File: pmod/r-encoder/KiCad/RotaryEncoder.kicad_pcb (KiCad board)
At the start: 2 copper layers, 39 x 39 mm, 15 parts, among them J1 Conn_01x06, U1 PEC11R-4325F-S0012

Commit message: fix: connectors
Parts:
- J1: footprint Connector_PinHeader_2.54mm:PinHeader_1x06_P2.54mm_Vertical -> Connector_PinHeader_2.54mm:PinHeader_1x06_P2.54mm_Horizontal
- moved J1 12.8 mm to (110.2, 80.1), turned to 180 degrees
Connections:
- J1 pad 1: A -> unconnected-(J1-Pin_1-Pad1)
- J1 pad 2: B -> BTN
- J1 pad 3: BTN -> B
- J1 pad 4: unconnected-(J1-Pin_4-Pad4) -> A
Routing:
- net GND: track 9.76 -> 0.00 mm, vias 17 -> 15
- net A: track 12.2 -> 17.3 mm
- net B: track 21.1 -> 17.7 mm
- net VCC: track 55.4 -> 54.8 mm
- net BTN: track 32.9 -> 33.2 mm, vias 0 -> 1

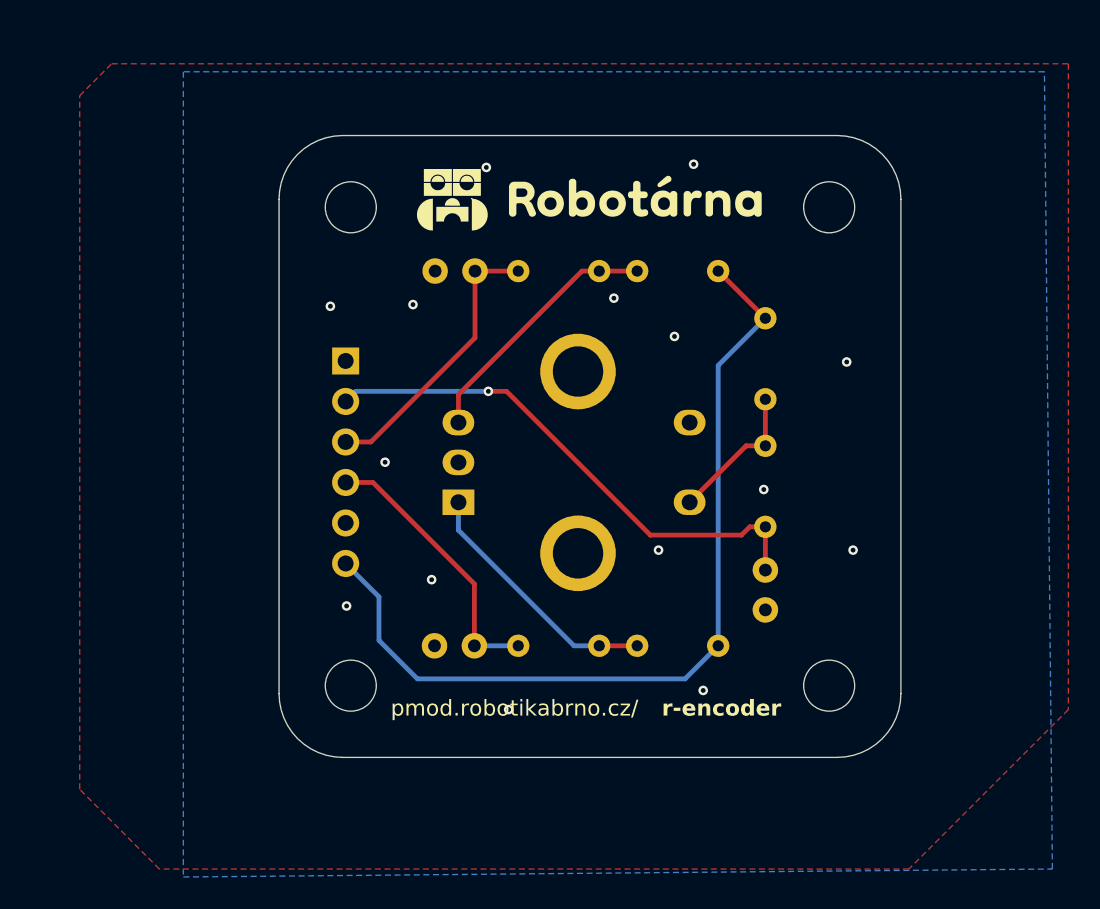
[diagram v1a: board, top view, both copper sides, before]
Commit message: fix: prepare all board for manufacturing
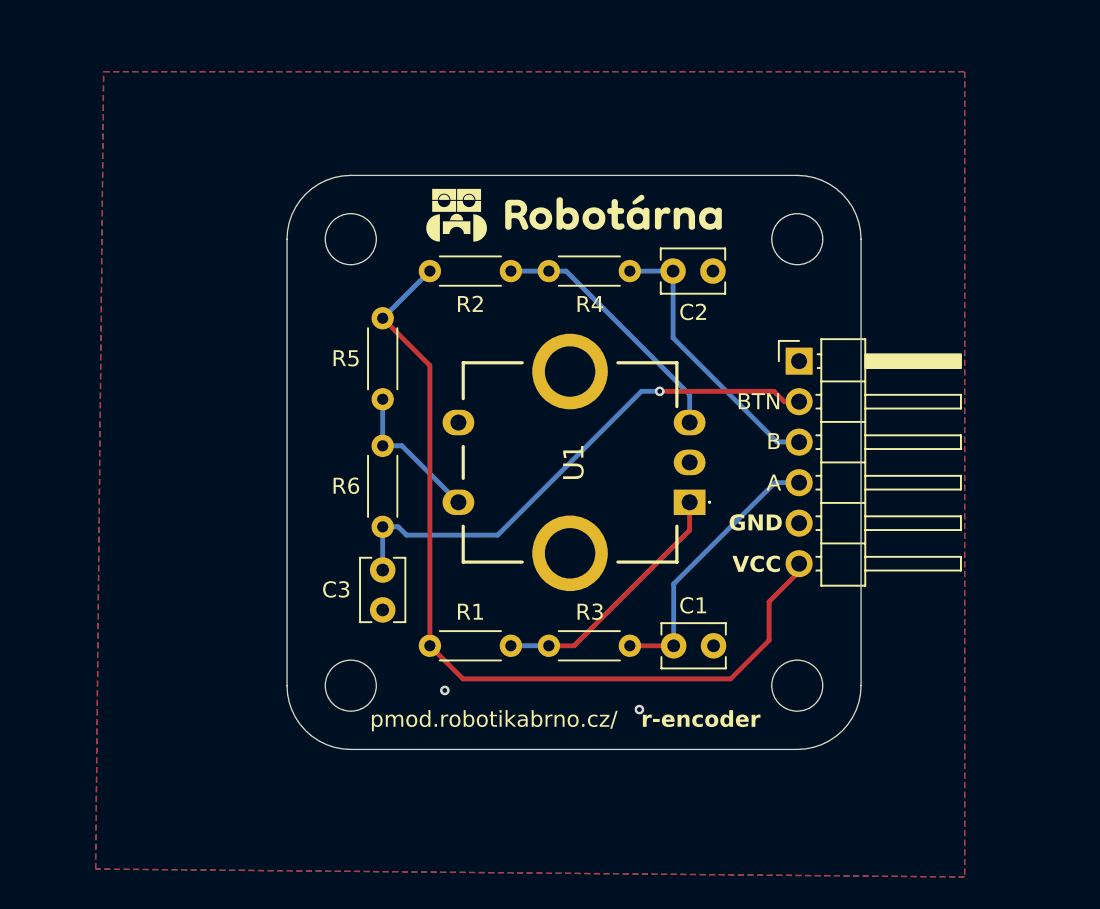
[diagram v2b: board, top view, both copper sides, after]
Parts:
- C1, C2, C3: value 0.01uF -> 10nF; moved to F.Cu
- H1, H2, H3, H4: moved to B.Cu
- J1, R1, R2, R3, R4, R5, R6, U1: moved to F.Cu
- moved H1 30.1 mm to (110.5, 72.5), turned to 180 degrees
- moved H3 30.0 mm to (110.5, 100.5), turned to 180 degrees
- moved J1 28.4 mm to (138.6, 80.2), turned to 0 degrees
- moved H2 28.1 mm to (138.5, 72.5), turned to 180 degrees
- moved H4 28.0 mm to (138.5, 100.5), turned to 180 degrees
- moved C3 24.0 mm to (112.5, 93.2)
- moved R5 24.0 mm to (112.5, 82.5)
- moved R6 24.0 mm to (112.5, 85.5)
- moved R1 18.1 mm to (115.5, 98.0), turned to 0 degrees
- moved R2 18.1 mm to (115.5, 74.5), turned to 0 degrees
- moved C1 17.5 mm to (133.2, 98.0), turned to 180 degrees
- moved C2 17.4 mm to (133.2, 74.5), turned to 180 degrees
- moved U1 14.5 mm to (131.8, 89.0)
- moved R4 7.00 mm to (128.0, 74.5), turned to 180 degrees
- moved R3 3.16 mm to (122.9, 98.0), turned to 0 degrees
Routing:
- net A: track 17.3 -> 17.9 mm
- net BTN: track 33.2 -> 33.8 mm
- net GND: vias 15 -> 2
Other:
- board size 39 x 39 mm -> 36 x 36 mm
- board text added: "36mm"
- board text removed: "30mm"
- board text removed: "M3"

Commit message: docs: add images, fix docs
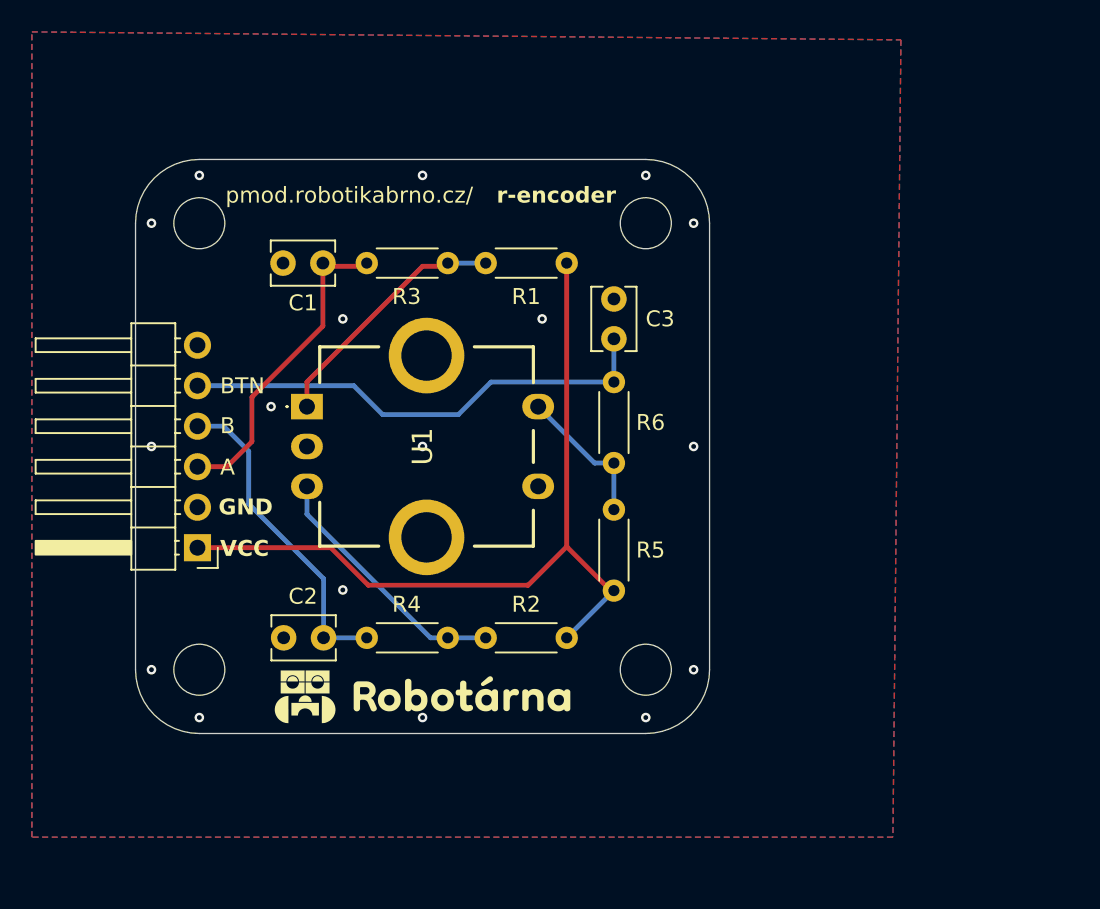
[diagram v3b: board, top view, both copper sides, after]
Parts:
- moved H4 47.4 mm to (101.0, 71.5), turned to 0 degrees
- moved H2 46.2 mm to (101.0, 99.5), turned to 0 degrees
- moved J1 39.5 mm to (100.9, 91.8), turned to 180 degrees
- moved C1 36.1 mm to (106.2, 74.0), turned to 0 degrees
- moved C2 35.4 mm to (106.3, 97.5), turned to 0 degrees
- moved H3 34.4 mm to (129.0, 71.5), turned to 0 degrees
- moved H1 32.7 mm to (129.0, 99.5), turned to 0 degrees
- moved R4 28.3 mm to (111.5, 97.5), turned to 0 degrees
- moved R1 25.5 mm to (124.0, 74.0), turned to 180 degrees
- moved R3 24.8 mm to (116.6, 74.0), turned to 180 degrees
- moved U1 24.7 mm to (107.8, 83.0), turned to -90 degrees
- moved R2 24.5 mm to (124.0, 97.5), turned to 180 degrees
- moved C3 20.5 mm to (127.0, 78.8), turned to 90 degrees
- moved R5 16.1 mm to (127.0, 89.5), turned to -90 degrees
- moved R6 14.5 mm to (127.0, 86.5), turned to 90 degrees
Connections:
- J1 pad 1: unconnected-(J1-Pin_1-Pad1) -> VCC
- J1 pad 2: BTN -> GND
- J1 pad 3: B -> A
- J1 pad 4: A -> B
- J1 pad 5: GND -> BTN
- J1 pad 6: VCC -> unconnected-(J1-Pin_6-Pad6)
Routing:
- net VCC: track 54.9 -> 51.1 mm
- net BTN: track 33.8 -> 30.4 mm, vias 1 -> 0
- net B: track 18.0 -> 20.5 mm
- net A: track 17.9 -> 19.9 mm
- net GND: track 0.00 -> 0.28 mm, vias 2 -> 17
